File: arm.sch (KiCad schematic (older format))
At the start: 99 parts, among them J1 MICROSD_SOCKET_SPI, M1 MOTOR, P1 MicroUSB, P2 HC-05/06, Q1 MOSFET_N, Q2 IRLML2246TRPBF, Q3 IRLML2246TRPBF, Q5 IRLML2246TRPBF, Q6 IRLML2246TRPBF, Q7 IRLML2246TRPBF, Q8 IRLML2246TRPBF, Q9 IRLML2246TRPBF, U3 LTC2942-1, U4 HMC5883L, U5 MPU6050, U7 BMP085, X1 8 mHz, X2 32.768(MS3V-T1R)

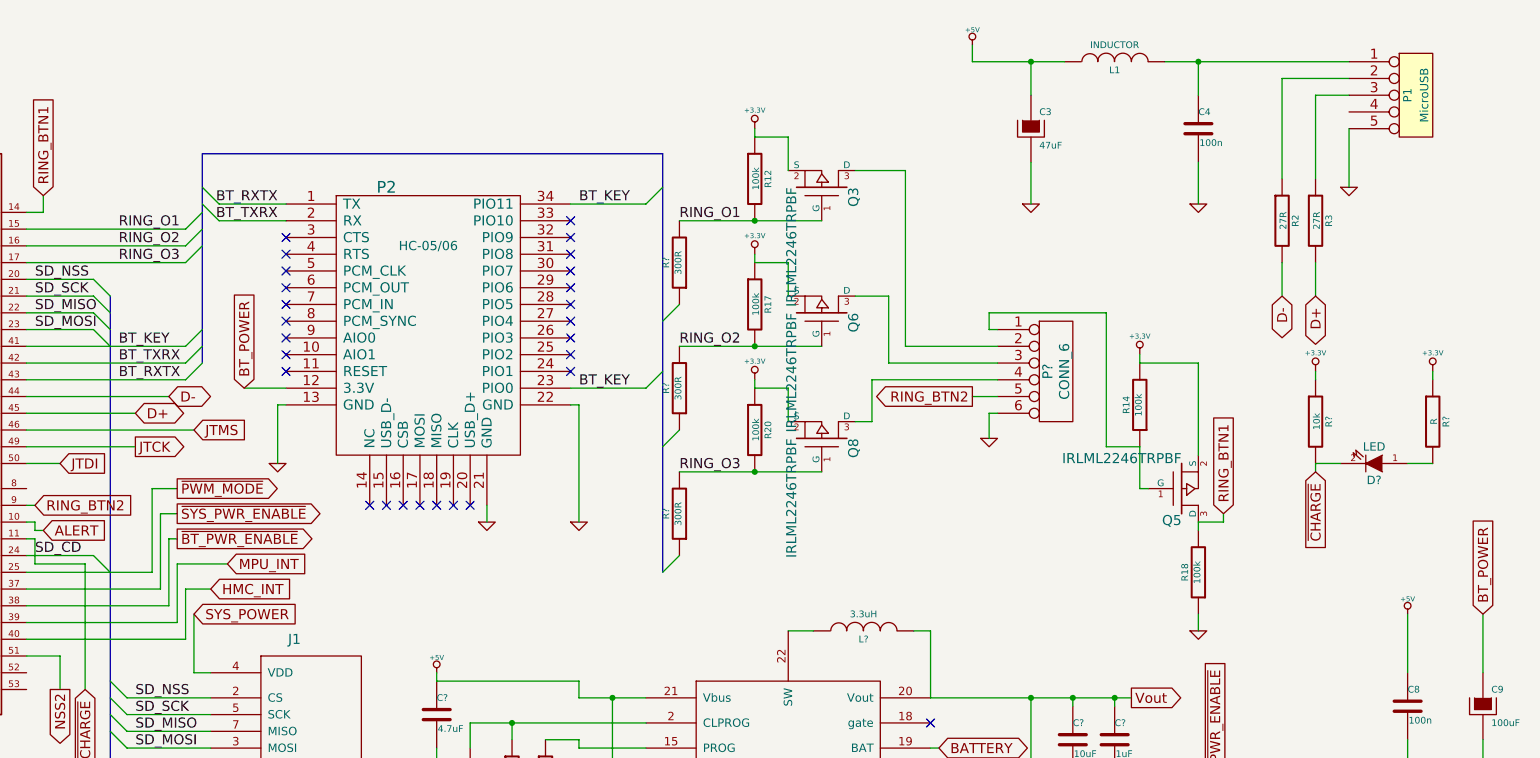
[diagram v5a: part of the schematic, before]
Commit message: Fixed LED bus names
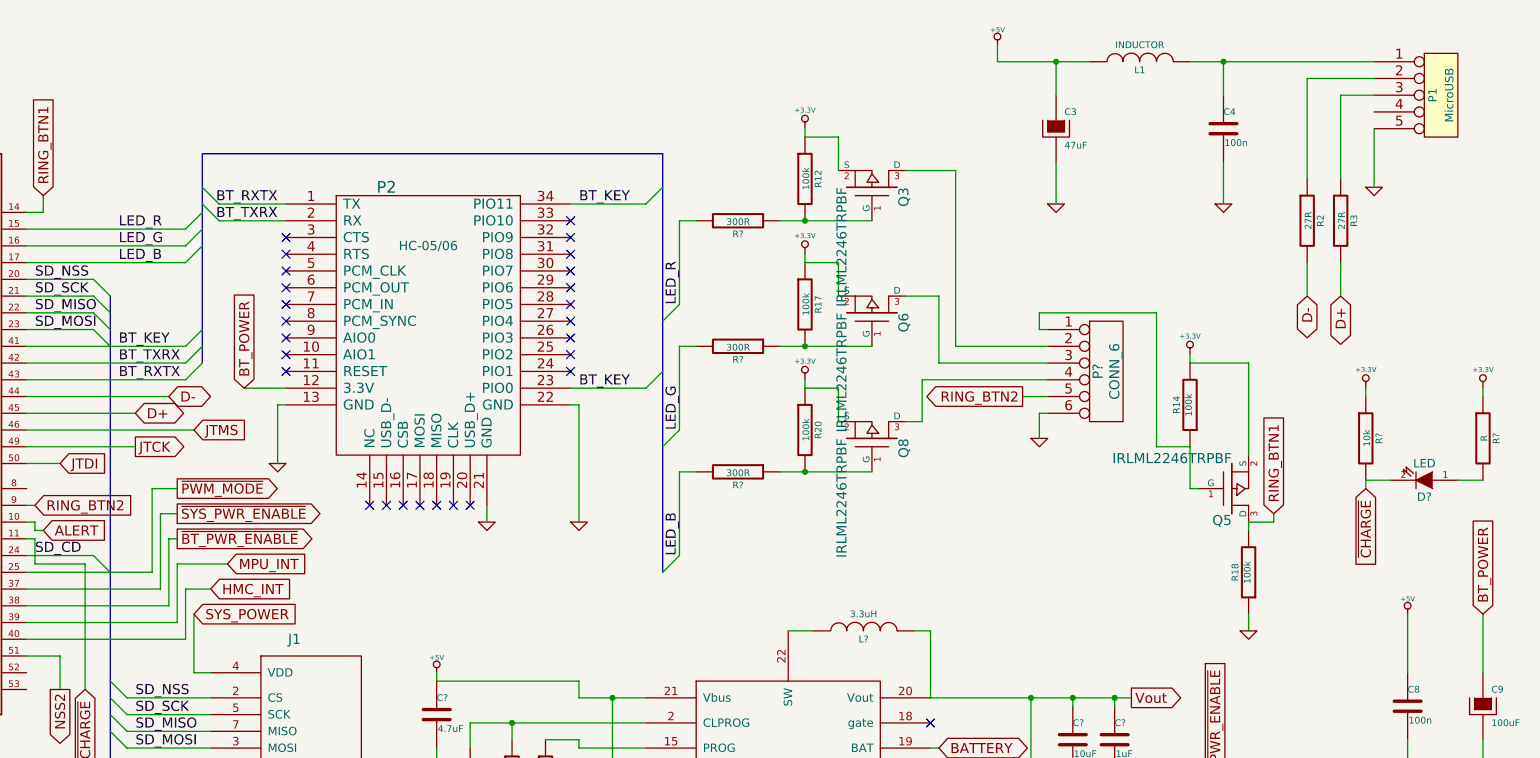
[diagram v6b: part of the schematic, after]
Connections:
- net at R?.1: now also Q3.1 (G), R12.2
- net at R?.1: now also Q6.1 (G), R17.2
- net at R?.1: now also Q8.1 (G), R20.2
- net RING_O1 renamed LED_R
- net LED_R: no longer Q3.1 (G), R12.2
- net RING_O2 renamed LED_G
- net LED_G: no longer Q6.1 (G), R17.2
- net RING_O3 renamed LED_B
- net LED_B: no longer Q8.1 (G), R20.2
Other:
- moved on the sheet: C3, C4, D?, L1, P1, P?, Q3, Q5, Q6, Q8, R12, R14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

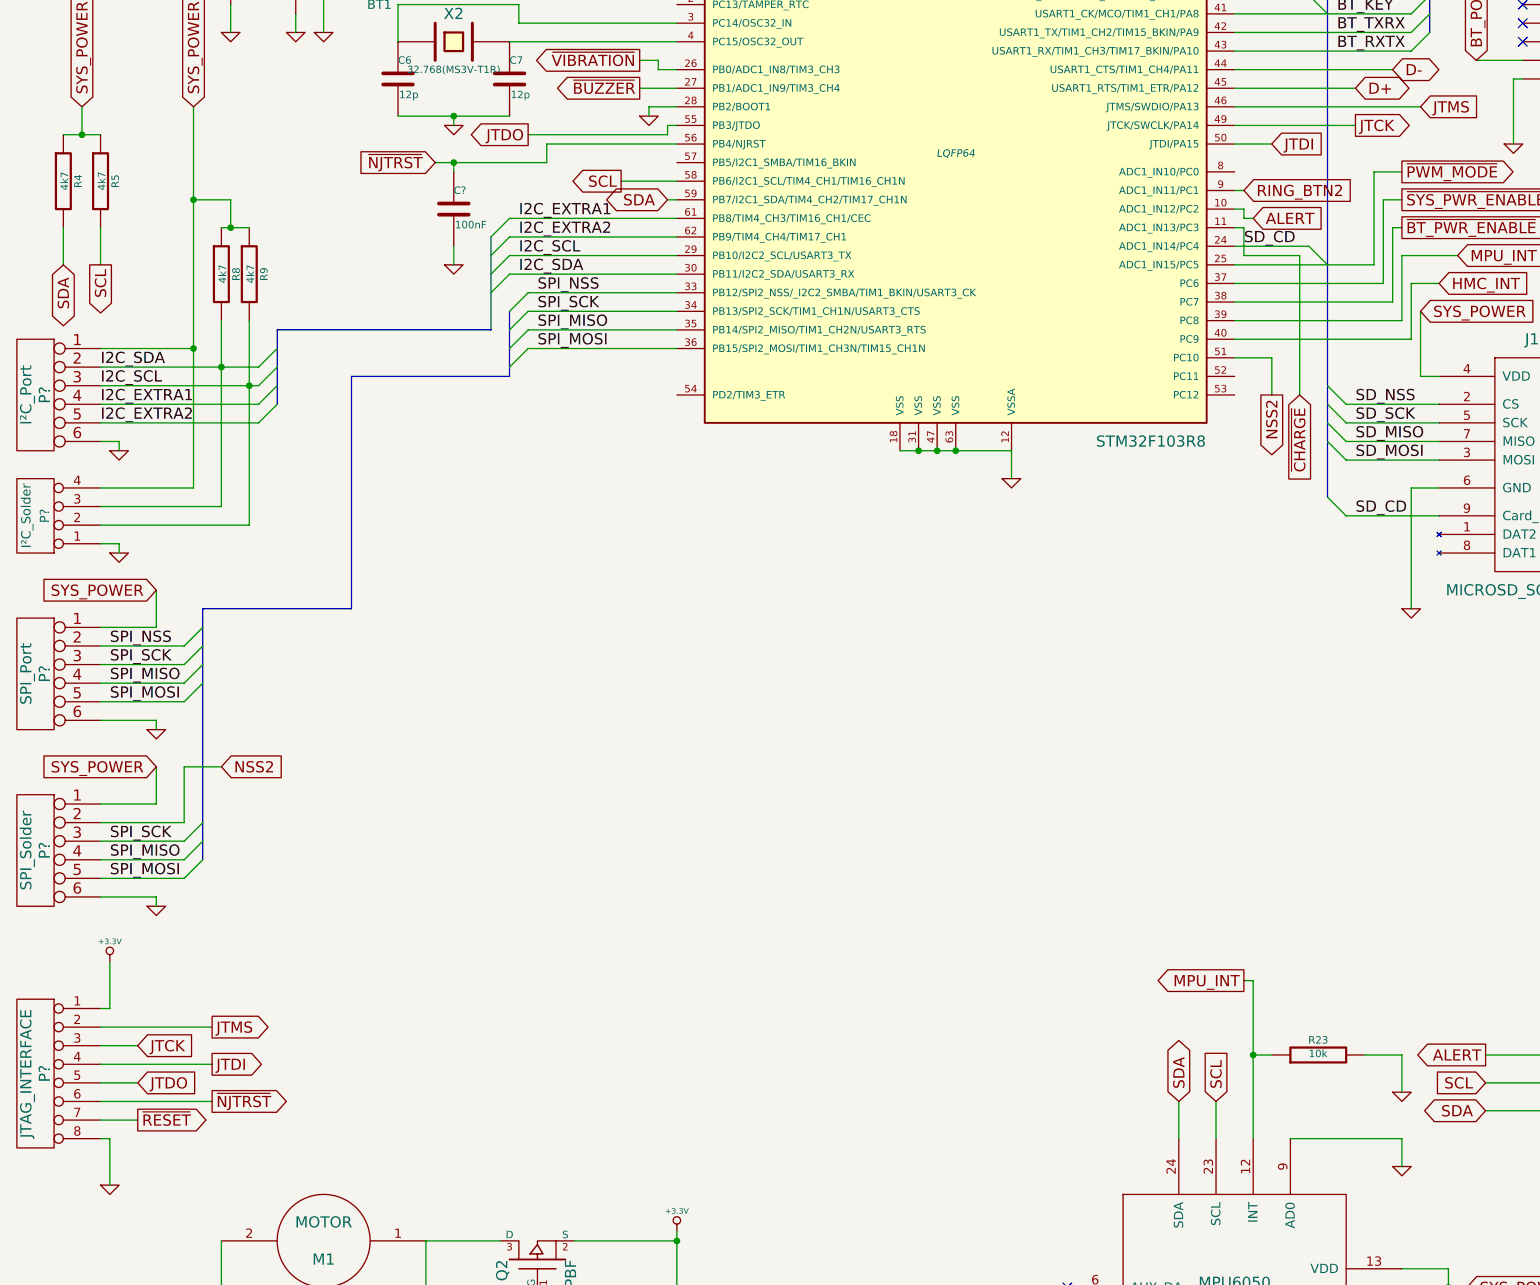
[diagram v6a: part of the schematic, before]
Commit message: Not connected pins, minor fixes
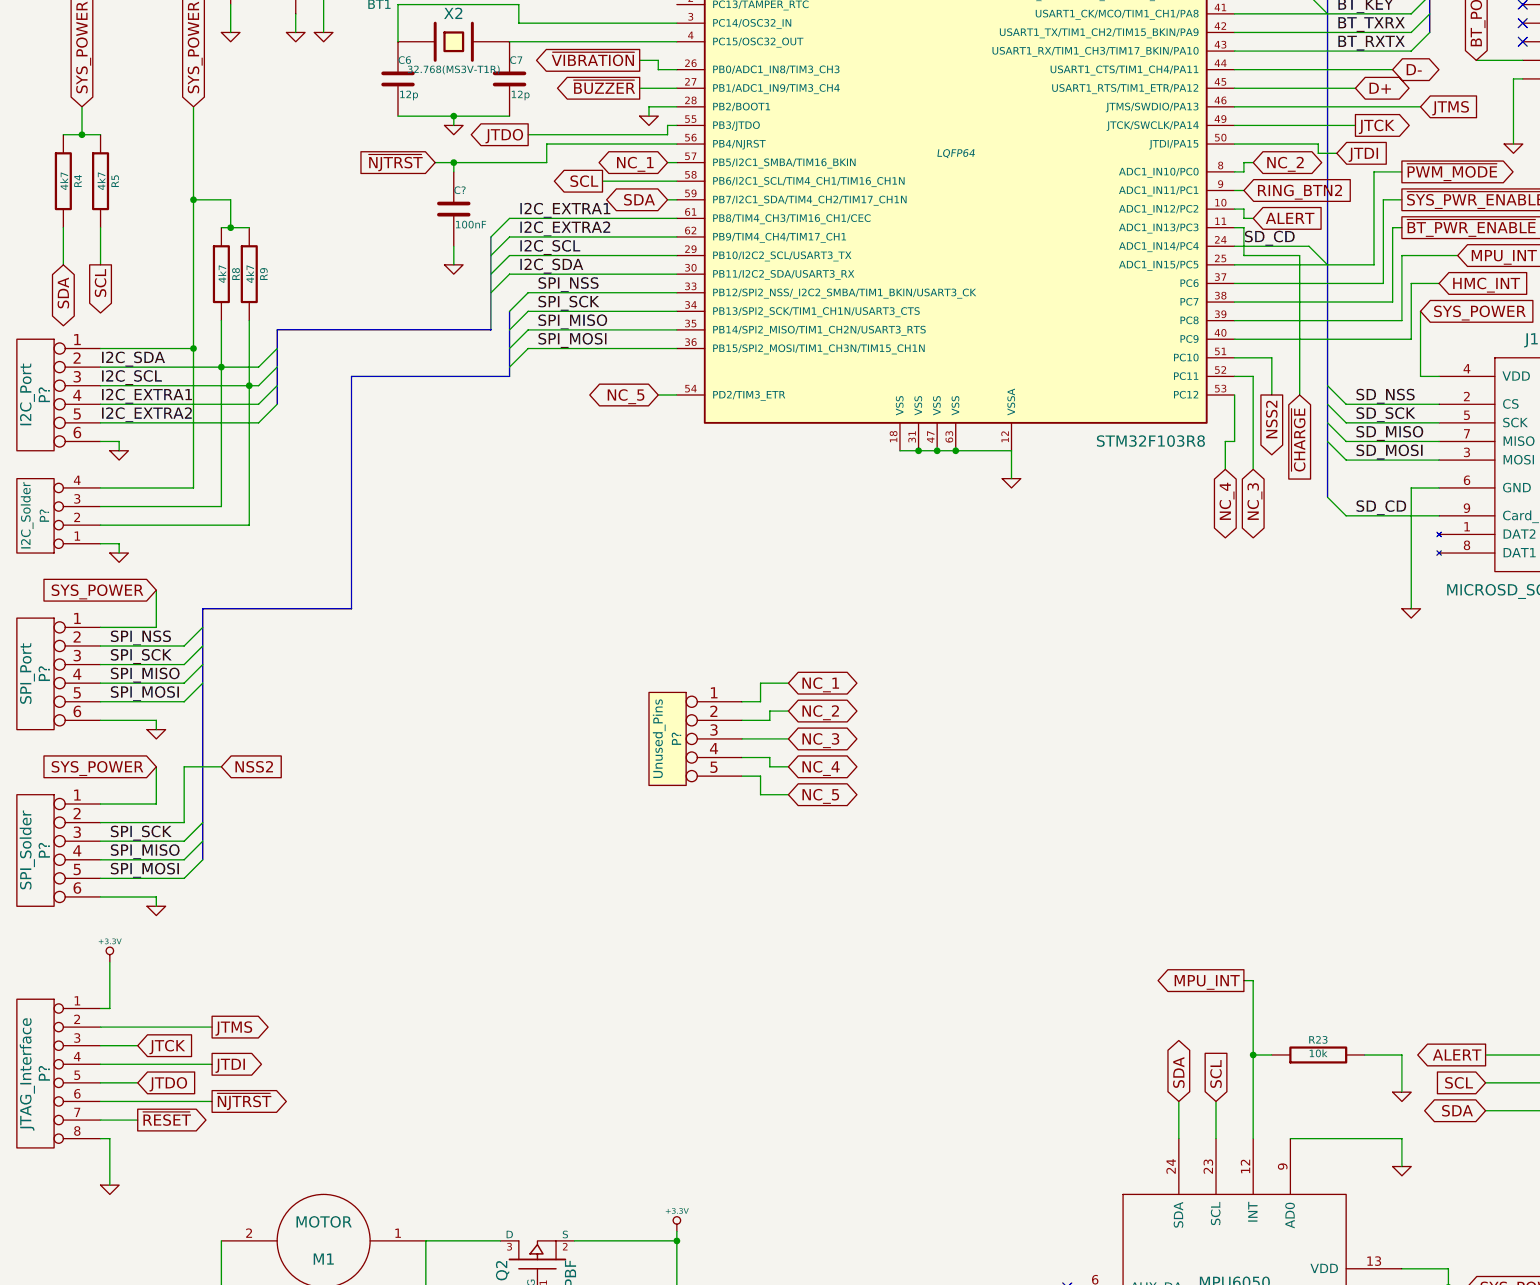
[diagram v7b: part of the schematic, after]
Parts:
- added P?: Unused_Pins, symbol CONN_5
- P?: value I²C_Solder -> I2C_Solder
- P?: value I²C_Port -> I2C_Port
- P?: value JTAG_INTERFACE -> JTAG_Interface
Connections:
- net NC_3: now reaches U?.52 (PC11)
- net NC_3: now also P?.3
- net NC_4: now reaches U?.53 (PC12)
- net NC_4: now also P?.4
- net NC_5: now reaches U?.54 (PD2/TIM3_ETR)
- net NC_5: now also P?.5
- net NC_1: now reaches U?.57 (PB5/I2C1_SMBA/TIM16_BKIN)
- net NC_1: now also P?.1
- net NC_2: now reaches U?.8 (ADC1_IN10/PC0)
- net NC_2: now also P?.2
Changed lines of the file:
@@
 Text GLabel 4050 3450 0    60   BiDi ~ 0
 SDA
-Text GLabel 3800 3350 0    60   Output ~ 0
+Text GLabel 3700 3350 0    60   Output ~ 0
 SCL
 $Comp
@@
 P 650 5150
 F 0 "P?" V 600 5150 50  0000 C CNN
-F 1 "I²C_Solder" V 700 5150 50  0000 C CNN
+F 1 "I2C_Solder" V 700 5150 50  0000 C CNN
 F 2 "" H 650 5150 60  0000 C CNN
 F 3 "" H 650 5150 60  0000 C CNN
@@
 P 650 4500
 F 0 "P?" V 600 4500 60  0000 C CNN
-F 1 "I²C_Port" V 700 4500 60  0000 C CNN
+F 1 "I2C_Port" V 700 4500 60  0000 C CNN
 F 2 "" H 650 4500 60  0000 C CNN
 F 3 "" H 650 4500 60  0000 C CNN
@@
 Text GLabel 7750 3050 2    60   Output ~ 0
 JTCK
-Text GLabel 7300 3150 2    60   Input ~ 0
+Text GLabel 7650 3200 2    60   Input ~ 0
 JTDI
 Text GLabel 8100 2950 2    60   Input ~ 0
@@
 P 650 8150
 F 0 "P?" V 600 8150 60  0000 C CNN
-F 1 "JTAG_INTERFACE" V 700 8150 60  0000 C CNN
+F 1 "JTAG_Interface" V 700 8150 60  0000 C CNN
 F 2 "" H 650 8150 60  0000 C CNN
 F 3 "" H 650 8150 60  0000 C CNN
@@
 	4050 3450 4100 3450
 Wire Wire Line
-	3800 3350 4100 3350
+	3700 3350 4100 3350
 Wire Wire Line
 	2200 2200 2200 2550
@@
 	7850 3800 7100 3800
 Wire Wire Line
-	7300 3150 7100 3150
+	7550 3150 7100 3150
 Wire Wire Line
 	7100 3050 7750 3050
@@
 Wire Wire Line
 	11000 3200 11000 3700
+Text GLabel 4050 3250 0    60   BiDi ~ 0
+NC_1
+Wire Wire Line
+	4050 3250 4100 3250
+Text GLabel 7200 3250 2    60   BiDi ~ 0
+NC_2
+Wire Wire Line
+	7100 3300 7150 3300
+Wire Wire Line
+	7150 3300 7150 3250
+Wire Wire Line
+	7150 3250 7200 3250
+Wire Wire Line
+	7550 3150 7550 3200
+Wire Wire Line
+	7550 3200 7650 3200
+Wire Wire Line
+	7100 4400 7200 4400
+Wire Wire Line
+	7200 4400 7200 4900
+Wire Wire Line
+	7100 4500 7100 4750
+Text GLabel 7200 4900 3    60   BiDi ~ 0
+NC_3
+Text GLabel 7050 4900 3    60   BiDi ~ 0
+NC_4
+Wire Wire Line
+	7100 4750 7050 4750
+Wire Wire Line
+	7050 4750 7050 4900
+Text GLabel 4000 4500 0    60   BiDi ~ 0
+NC_5
+Wire Wire Line
+	4000 4500 4100 4500
+$Comp
+L CONN_5 P?
+U 1 1 53A2540D
+P 4050 6350
+F 0 "P?" V 4000 6350 50  0000 C CNN
+F 1 "Unused_Pins" V 4100 6350 50  0000 C CNN
+F 2 "" H 4050 6350 60  0000 C CNN
+F 3 "" H 4050 6350 60  0000 C CNN
+	1    4050 6350
+	-1   0    0    -1
+$EndComp
+Text GLabel 4700 6050 2    60   BiDi ~ 0
+NC_1
+Text GLabel 4700 6200 2    60   BiDi ~ 0
+NC_2
+Text GLabel 4700 6350 2    60   BiDi ~ 0
+NC_3
+Text GLabel 4700 6500 2    60   BiDi ~ 0
+NC_4
+Text GLabel 4700 6650 2    60   BiDi ~ 0
+NC_5
+Wire Wire Line
+	4450 6150 4550 6150
+Wire Wire Line
+	4550 6150 4550 6050
+Wire Wire Line
+	4550 6050 4700 6050
+Wire Wire Line
+	4450 6250 4600 6250
+Wire Wire Line
+	4600 6250 4600 6200
+Wire Wire Line
+	4600 6200 4700 6200
+Wire Wire Line
+	4450 6350 4700 6350
+Wire Wire Line
+	4450 6450 4600 6450
+Wire Wire Line
+	4600 6450 4600 6500
+Wire Wire Line
+	4600 6500 4700 6500
+Wire Wire Line
+	4450 6550 4550 6550
+Wire Wire Line
+	4550 6550 4550 6650
+Wire Wire Line
+	4550 6650 4700 6650
 $EndSCHEMATC

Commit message: Automatic annotation, generated netlist
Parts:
- gave numbers to parts that had none: 40
- renumbered C5 to C1, C15 to C10, C16 to C11, C12 to C14, C17 to C15, C18 to C17, C3 to C18, C4 to C22, C8 to C23, C9 to C24, C11 to C25, C6 to C3, C1 to C5, C7 to C6, C2 to C7, C19 to C8, C20 to C9, FW/RST to FW/RST1, L1 to L3, P2 to P7, P1 to P9, Q7 to Q10, Q9 to Q11, Q2 to Q3, Q3 to Q4, Q6 to Q5, Q8 to Q6, Q5 to Q8, Q1 to Q9, R10 to R11, R23 to R12, R12 to R19, R4 to R2, R17 to R20, R20 to R21, R14 to R24, R15 to R25, R21 to R26, R18 to R27, R2 to R28, R3 to R29, R5 to R3, R19 to R30, R24 to R32, R8 to R4, R9 to R5, R7 to R9, U7 to U1, U5 to U3, U3 to U4, U4 to U5, X2 to X1, X1 to X2
